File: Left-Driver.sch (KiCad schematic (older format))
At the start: 4 parts

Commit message: Added the basic Schematic
PWM generators work for given reference design values. (LAB Tested)
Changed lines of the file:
@@
 LIBS:contrib
 LIBS:valves
-LIBS:Buck Supply-cache
 LIBS:H-Bridge PWM Switching Circuit-cache
 EELAYER 25 0
@@
 	3700 3050 4250 3050
 Wire Wire Line
-	3350 3100 3350 3200
-Wire Wire Line
-	3350 3200 3350 3400
+	3350 3100 3350 3400
 Wire Wire Line
 	4250 3200 3350 3200
 Connection ~ 3350 3200
 Wire Wire Line
-	3350 2800 3350 2750
-Wire Wire Line
-	3350 2750 3350 2150
-Wire Wire Line
-	3350 2150 3350 1950
+	3350 1950 3350 2800
 Wire Wire Line
 	4250 2750 3350 2750
@@
 $EndComp
 Wire Wire Line
-	5150 3050 6150 3050
+	5150 3050 6750 3050
 Wire Wire Line
-	6150 3050 6750 3050
-Wire Wire Line
-	6150 2750 5700 2750
-Wire Wire Line
-	5700 2750 5150 2750
+	5150 2750 6150 2750
 Wire Wire Line
 	4800 2150 5700 2150

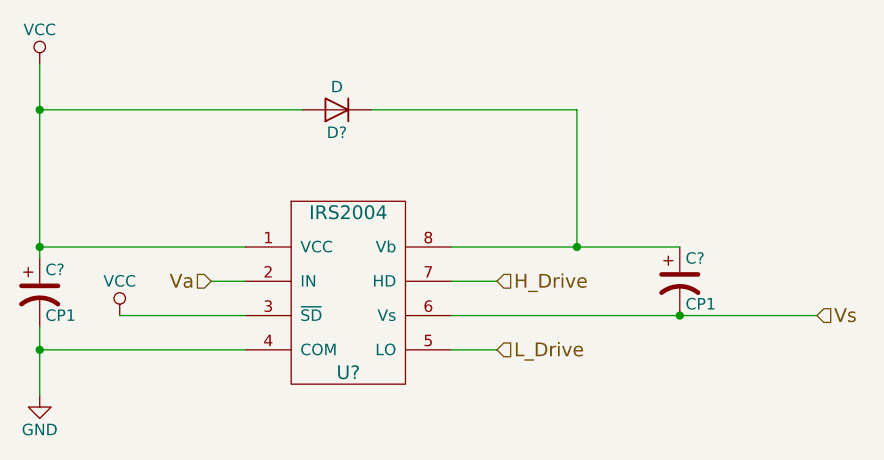
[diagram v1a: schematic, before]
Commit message: Updated the System pull-up resistors
Turns out that the IRS2004 requires a 1k pull up to work smoothly.
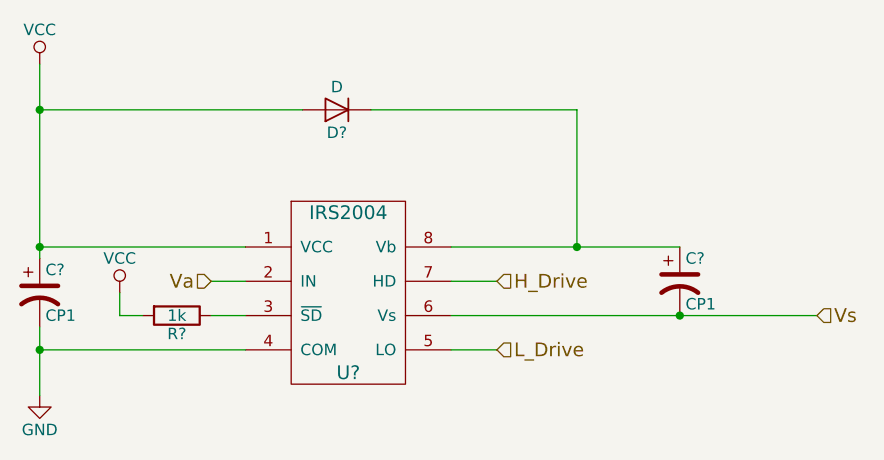
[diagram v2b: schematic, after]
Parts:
- added R?: 1k, symbol R
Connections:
- net VCC: now also R?.2; no longer U?.3 (~SD)
- new net: R?.1, U?.3 (~SD)
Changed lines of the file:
@@
 L VCC #PWR?
 U 1 1 58E4AE22
-P 3700 3050
-F 0 "#PWR?" H 3700 2900 50  0001 C CNN
-F 1 "VCC" H 3700 3200 50  0000 C CNN
-F 2 "" H 3700 3050 50  0000 C CNN
-F 3 "" H 3700 3050 50  0000 C CNN
-	1    3700 3050
+P 3700 2950
+F 0 "#PWR?" H 3700 2800 50  0001 C CNN
+F 1 "VCC" H 3700 3100 50  0000 C CNN
+F 2 "" H 3700 2950 50  0000 C CNN
+F 3 "" H 3700 2950 50  0000 C CNN
+	1    3700 2950
 	1    0    0    -1
 $EndComp
 Wire Wire Line
 	4250 2900 4100 2900
-Wire Wire Line
-	3700 3050 4250 3050
 Wire Wire Line
 	3350 3100 3350 3400
@@
 Vs
 Connection ~ 6150 3050
+$Comp
+L R R?
+U 1 1 58FE349B
+P 3950 3050
+F 0 "R?" V 4030 3050 50  0000 C CNN
+F 1 "1k" V 3950 3050 50  0000 C CNN
+F 2 "" V 3880 3050 50  0000 C CNN
+F 3 "" H 3950 3050 50  0000 C CNN
+	1    3950 3050
+	0    1    1    0
+$EndComp
+Wire Wire Line
+	3700 2950 3700 3050
+Wire Wire Line
+	3700 3050 3800 3050
+Wire Wire Line
+	4100 3050 4250 3050
 $EndSCHEMATC
